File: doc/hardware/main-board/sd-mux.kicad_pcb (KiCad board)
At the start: 2 copper layers, 50 x 114 mm, 52 parts, among them J1 USDCARD, P1 USB_OTG, P10 PINS 1,5x3, P2 629105136821, P3 61400416021, P4 61400416021, P5 IDC_02X04, P6 IDC_02X04, P7 PINS 1,5x3, P8 CONN_02X02, P9 CONN_02X02, Q1 IRF7606PBF, Q2 IRF7606PBF, Q3 IRF7606PBF, Q4 IRF7606PBF, Q5 2N7002, Q6 2N7002, Q7 IRF7606PBF, Q8 IRF7606PBF, U1 TS3USB30EDGSR, U2 FT245RL, U3 74AHC1G14, U4 TS3A27518E, U5 74AHC1G14

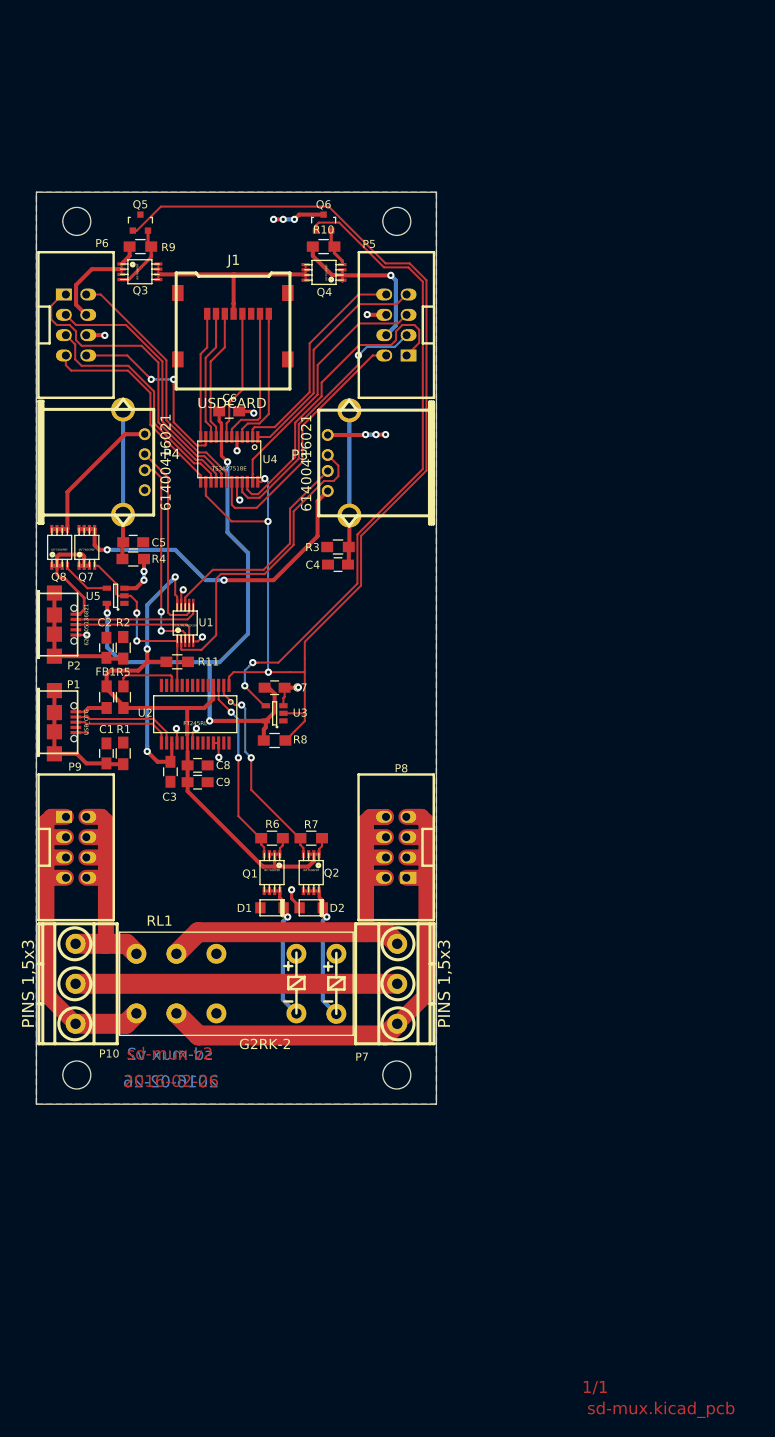
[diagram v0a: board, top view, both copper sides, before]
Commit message: Fix power supply connection of USB switch inverter
Power supply pin of U5 was connected to 3.3V. Q8, driven from this
inverter, couldn't be fully closed as maximum output voltage from
the inverter was 3.3V. Now, the inverter, is connected to VCC pin
of USB connector which gives 5V.

Change-Id: Ibed75765ea8cbc2727066d6a498a3396a2d3c404
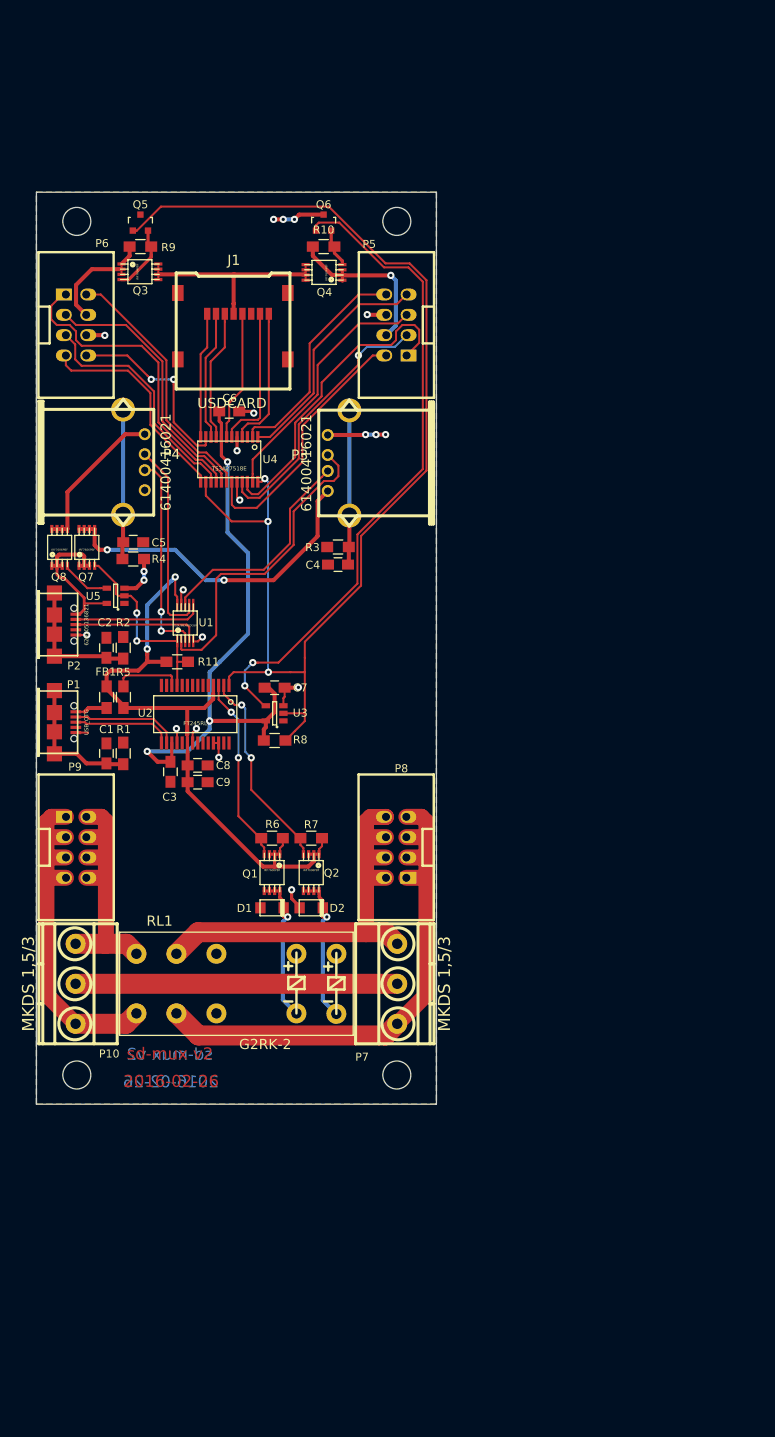
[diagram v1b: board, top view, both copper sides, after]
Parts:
- P10, P7: value PINS 1,5x3 -> MKDS 1,5/3
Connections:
- U5 pad 5: +3V3 -> Net-(P2-Pad1)
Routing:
- net +3V3: track 94.0 -> 73.1 mm, vias 4 -> 3
- net Net-(P2-Pad1): track 17.0 -> 19.9 mm

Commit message: Replace Micro SD card with SD card socket.  Add fiducials
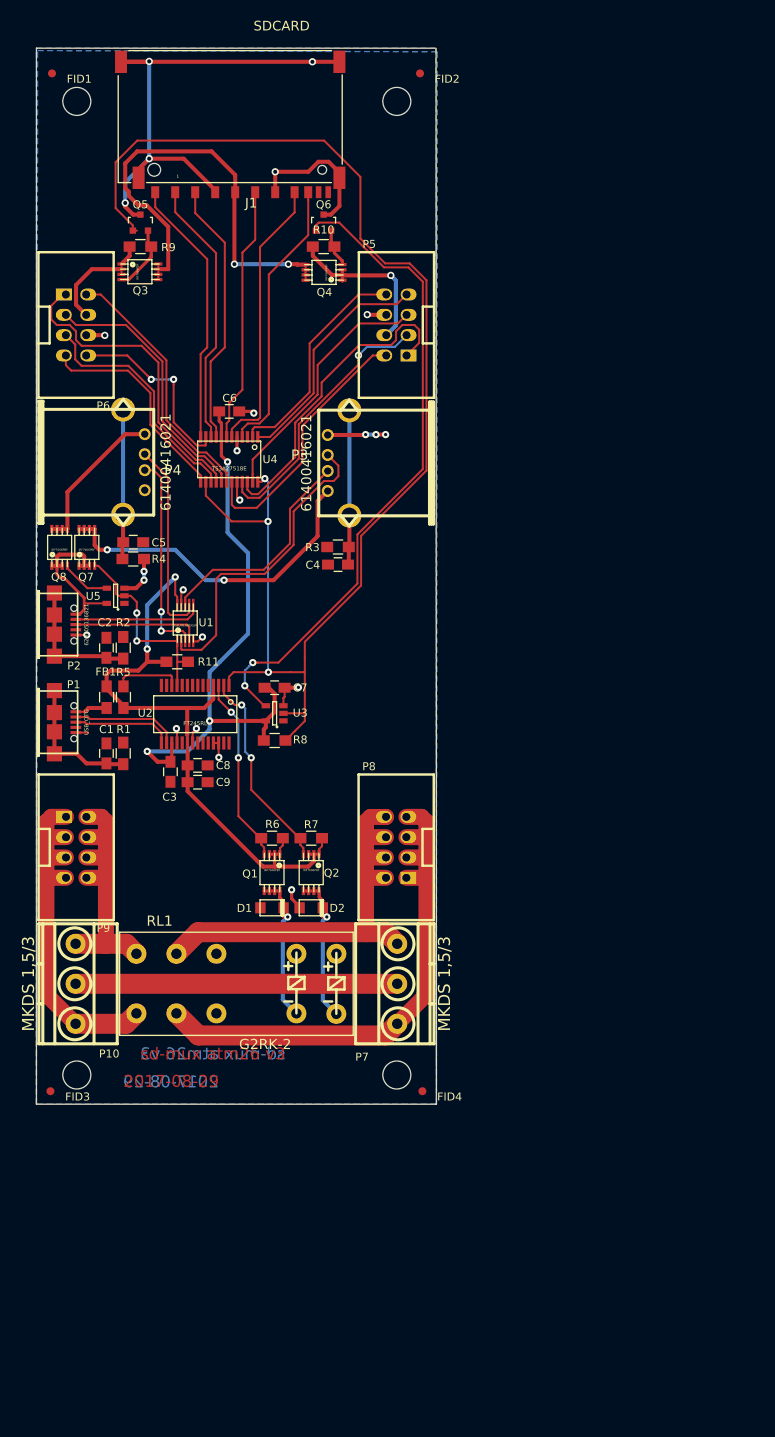
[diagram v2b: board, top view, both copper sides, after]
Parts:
- added FID1: Fiducial, Fiducials:Fiducial_1mm_Dia_2.54mm_Outer_CopperTop, F.Cu at (120.1, 18.8)
- added FID2: Fiducial, Fiducials:Fiducial_1mm_Dia_2.54mm_Outer_CopperTop, F.Cu at (166.1, 18.8)
- added FID3: Fiducial, Fiducials:Fiducial_1mm_Dia_2.54mm_Outer_CopperTop, F.Cu at (119.9, 146.0)
- added FID4: Fiducial, Fiducials:Fiducial_1mm_Dia_2.54mm_Outer_CopperTop, F.Cu at (166.4, 146.0)
- J1: value USDCARD -> SDCARD; footprint footprints:microsd_socket -> EAGLE-INPUT_OUTPUT_CONNECTORS-rev17c:693063020911
- P3, P4: footprint conn_usb_A -> footprints:conn_usb_A
- P5, P6: footprint footprint:PSB_IDC_4x2 -> footprints:PSB_IDC_4x2
- P8, P9: footprint footprints:PSB_IDC__4x2 -> footprints:PSB_IDC_4x2
- moved REF** 15.0 mm to (163.2, 22.3)
- moved REF** 15.0 mm to (123.2, 22.3)
- moved J1 14.5 mm to (142.4, 33.6)
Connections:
- net Net-(J1-Pad5) renamed /CLK
- net Net-(J1-Pad7) renamed /DAT0
- net Net-(J1-Pad8) renamed /DAT1
- J1 pad 1: Net-(J1-Pad1) -> /DAT3
- J1 pad 2: Net-(J1-Pad2) -> /CMD
- J1 pad 3: Net-(J1-Pad3) -> GND
- U4 pad 10: Net-(J1-Pad2) -> /DAT3
- U4 pad 12: Net-(J1-Pad1) -> /DAT2
- U4 pad 9: Net-(J1-Pad3) -> /CMD
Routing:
- net GND: track 49.3 -> 126.7 mm, vias 21 -> 23
- net /DAT2: track 0.00 -> 33.6 mm
- net /DAT3: track 0.00 -> 33.6 mm
- net /CMD: track 0.00 -> 33.2 mm
- net /USD_VDD: track 27.3 -> 57.0 mm, vias 0 -> 2
- net /SOCKET_SEL: track 156.4 -> 176.3 mm
- net /DAT1: track 17.6 -> 34.9 mm
- net /DAT0: track 18.1 -> 35.1 mm
- net Net-(J1-Pad3): track 16.4 -> 0.00 mm
- net Net-(J1-Pad2): track 16.3 -> 0.00 mm
- net /CLK: track 16.2 -> 32.1 mm
- net Net-(J1-Pad1): track 15.7 -> 0.00 mm
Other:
- board size 50 x 114 mm -> 50 x 132 mm
- net class Default: via_drill 0.4 -> 0.5
- net class USB_VCC: via_drill 0.4 -> 0.5
- net class VDD: via_drill 0.4 -> 0.5
- rule via_min_drill: 0.4 -> 0.5
- board text added: "2017-08-29"
- board text added: "sd-mux atm26 v3"
- board text removed: "2016-02-26"
- board text removed: "sd-mux v2"

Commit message: Make all vias 0.5mm.  Re-lay relay tracks for better isolation
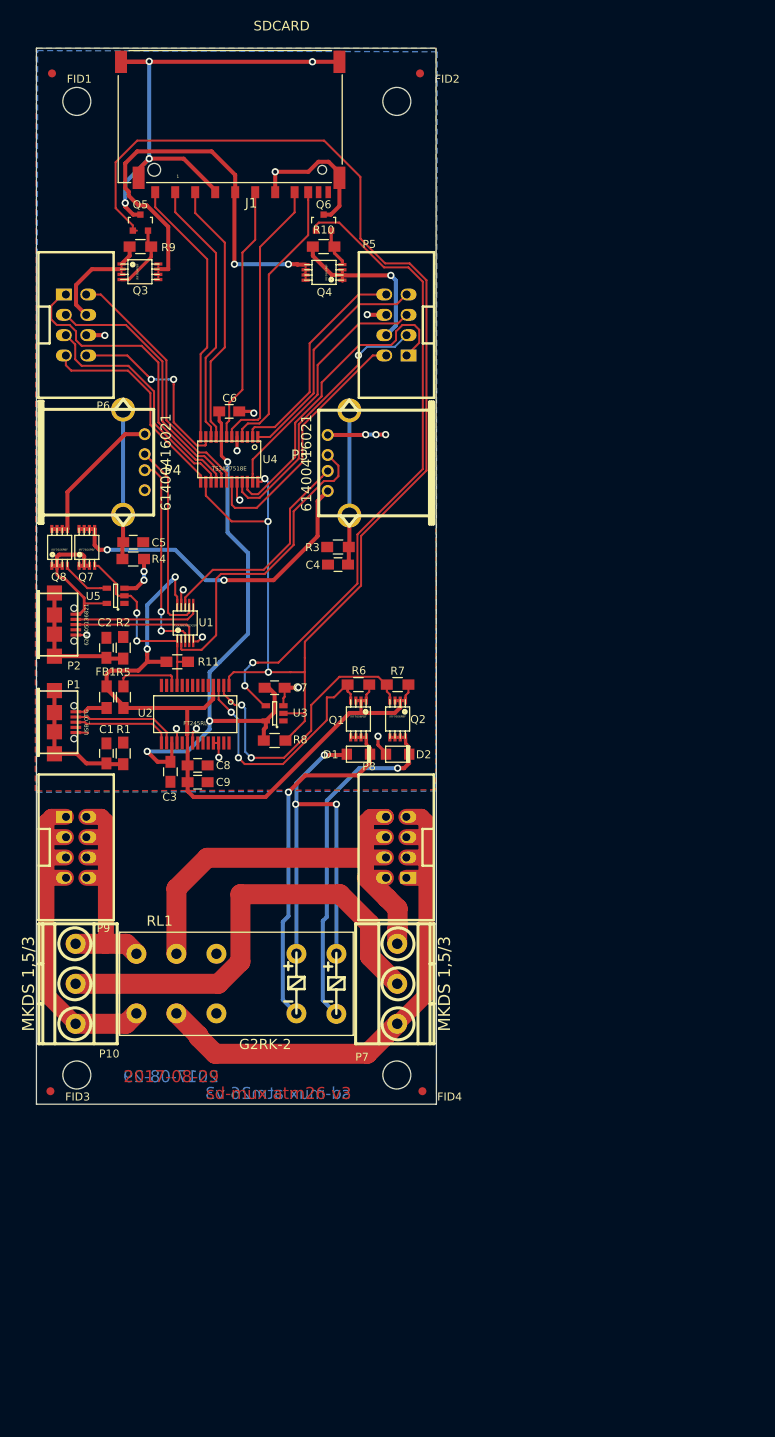
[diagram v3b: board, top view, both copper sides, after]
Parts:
- moved D1 22.0 mm to (158.4, 103.8)
- moved D2 22.0 mm to (163.3, 103.8)
- moved Q1 22.0 mm to (158.4, 99.5)
- moved Q2 22.0 mm to (163.3, 99.5)
- moved R6 22.0 mm to (158.4, 95.2)
- moved R7 22.0 mm to (163.3, 95.2)
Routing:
- net GND: track 126.7 -> 179.7 mm, vias 23 -> 26
- net Net-(D1-Pad1): track 18.9 -> 45.7 mm
- net Net-(D2-Pad1): track 18.9 -> 45.2 mm
- net Net-(P10-Pad2): track 40.2 -> 56.8 mm
- net VDD: track 81.5 -> 93.1 mm
- net /POWER_SW_ON: track 25.8 -> 36.5 mm
- net /POWER_SW_OFF: track 23.5 -> 32.9 mm
- net Net-(P7-Pad3): track 53.5 -> 60.8 mm
- net Net-(P7-Pad1): track 66.7 -> 68.7 mm

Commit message: Refactor relay section so that it obeys mains isolation.  Delete headers, rearrange so that 'live' and 'neutral' sections are separated.  Rejig pinout so that unused pins never become live, and rotate terminals so that they can be accesed from the end of the board.
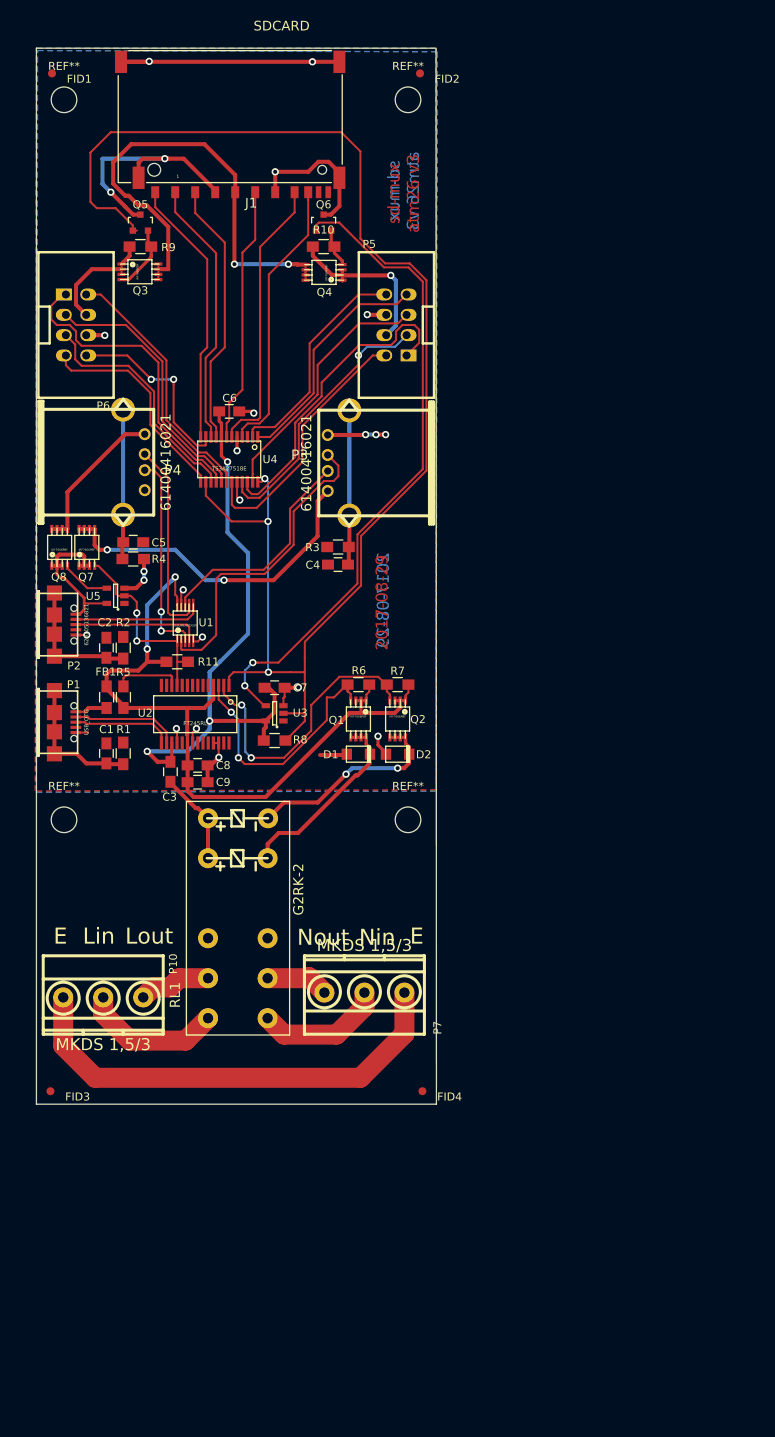
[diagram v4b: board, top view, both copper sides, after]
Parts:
- removed P8, P9: CONN_02X02, footprints:PSB_IDC_4x2
- removed the REF** at (163.2, 22.3)
- removed the REF** at (123.2, 22.3)
- removed the REF** at (123.2, 143.9)
- removed the REF** at (163.2, 143.9)
- added REF**: MountingHole_3.2mm_M3, Mounting_Holes:MountingHole_3.2mm_M3, F.Cu at (121.6, 22.1)
- added REF**: MountingHole_3.2mm_M3, Mounting_Holes:MountingHole_3.2mm_M3, F.Cu at (164.6, 112.1)
- added REF**: MountingHole_3.2mm_M3, Mounting_Holes:MountingHole_3.2mm_M3, F.Cu at (164.6, 22.1)
- added REF**: MountingHole_3.2mm_M3, Mounting_Holes:MountingHole_3.2mm_M3, F.Cu at (121.6, 112.1)
- moved RL1 8.20 mm to (143.4, 124.4), turned to 270 degrees
- moved P7 4.25 mm to (159.2, 133.7), turned to 180 degrees
- moved P10 3.85 mm to (126.5, 134.3), turned to 0 degrees
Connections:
- P10 pad 1: Net-(P10-Pad1) -> /E
- P10 pad 2: Net-(P10-Pad2) -> /Lin
- P10 pad 3: Net-(P10-Pad3) -> /Lout
- P7 pad 1: Net-(P7-Pad1) -> /E
- P7 pad 2: Net-(P10-Pad2) -> /Nin
- P7 pad 3: Net-(P7-Pad3) -> /Nout
- RL1 pad 4: Net-(P7-Pad1) -> /Nout
- RL1 pad 5: Net-(P10-Pad3) -> /Nin
- RL1 pad 6: Net-(P10-Pad1) -> /Lin
- RL1 pad 7: Net-(P7-Pad3) -> /Lout
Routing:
- net Net-(P7-Pad1): track 68.7 -> 0.00 mm
- net Net-(P7-Pad3): track 60.8 -> 0.00 mm
- net /E: track 0.00 -> 57.8 mm
- net Net-(P10-Pad2): track 56.8 -> 0.00 mm
- net Net-(P10-Pad3): track 45.1 -> 0.00 mm
- net GND: track 179.7 -> 143.3 mm, vias 26 -> 23
- net Net-(P10-Pad1): track 33.6 -> 0.00 mm
- net Net-(D1-Pad1): track 45.7 -> 24.1 mm, vias 1 -> 0
- net Net-(D2-Pad1): track 45.2 -> 25.9 mm, vias 1 -> 2
- net /Lin: track 0.00 -> 17.7 mm
- net /Nin: track 0.00 -> 16.2 mm
- net /SOCKET_SEL: track 176.3 -> 185.6 mm
- net /Lout: track 0.00 -> 9.09 mm
- net /Nout: track 0.00 -> 7.97 mm
- net /USD_VDD: track 57.0 -> 60.2 mm
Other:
- board text added: "E"
- board text added: "Lin"
- board text added: "Lout"
- board text added: "Nin"
- board text added: "Nout"
